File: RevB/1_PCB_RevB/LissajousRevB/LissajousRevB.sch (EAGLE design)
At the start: 77 parts, among them U101 LM348D, U201 LM348D, U401 LM348D

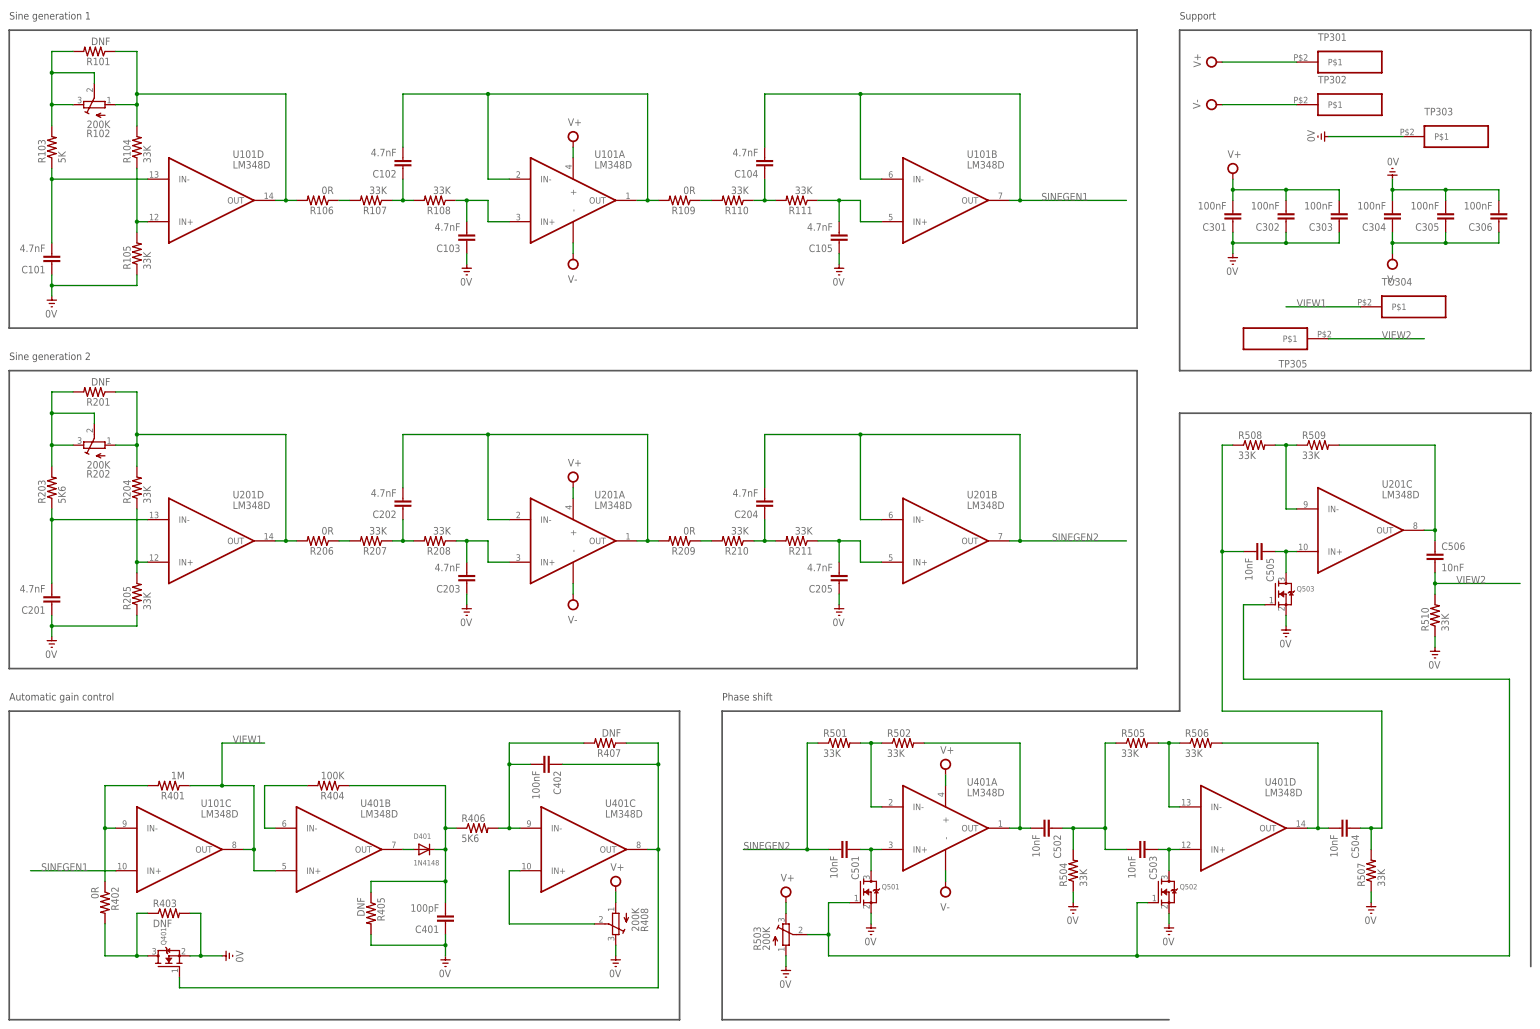
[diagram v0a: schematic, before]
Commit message: down to one quad op-amp package
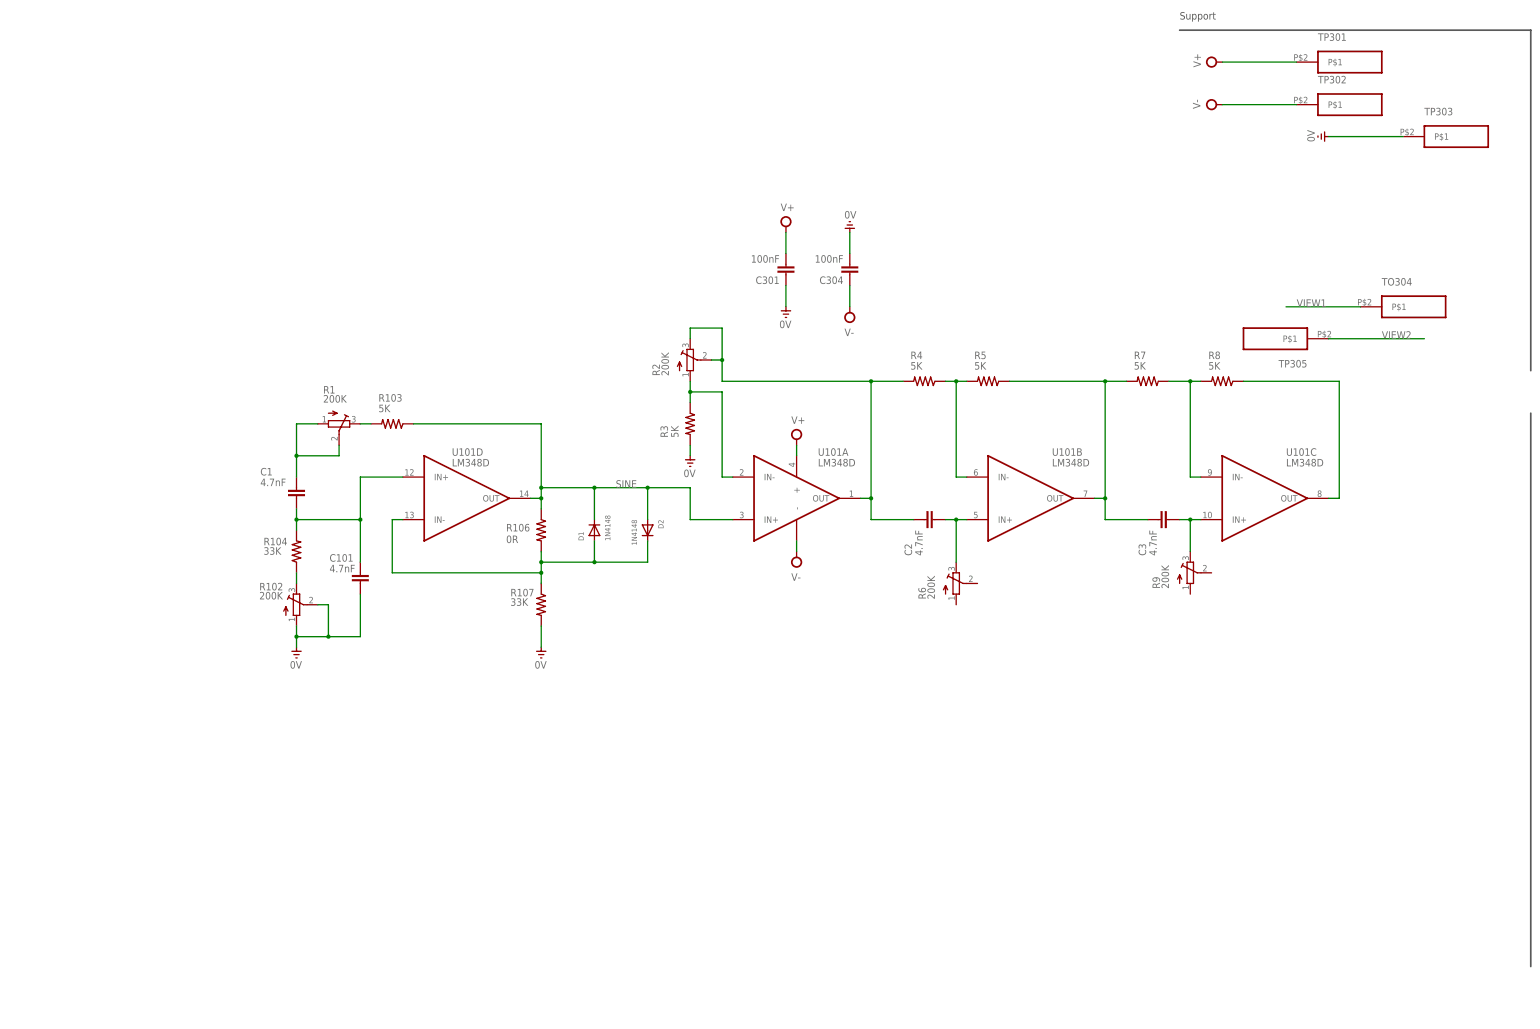
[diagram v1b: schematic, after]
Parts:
- removed C102, C103, C104, C105, C201, C202, C203, C204, C205: 4.7nF, passives:CAP0603-CAP
- removed C302, C303, C305, C306, C402: 100nF, passives:CAP0603-CAP
- removed C401: 100pF, passives:CAP0603-CAP
- removed C501, C502, C503, C504, C505, C506: 10nF, passives:CAP0603-CAP
- removed D401: 1N4148, adafruit:DIODESMA
- removed Q401, Q501, Q502, Q503: (no value), adafruit:MOSFET-NREFLOW
- removed R101, R201, R403, R405, R407: DNF, passives:RESISTOR0603-RES
- removed R105, R108, R110, R111, R204, R205, R207, R208, R210, R211, R501, R502, R504, R505, R506, R507, R508, R509, R510: 33K, passives:RESISTOR0603-RES
- removed R109, R206, R209, R402: 0R, passives:RESISTOR0603-RES
- removed R202, R408, R503: 200K, adafruit:TRIMPOTTC33X
- removed R203, R406: 5K6, passives:RESISTOR0603-RES
- removed R401: 1M, passives:RESISTOR0603-RES
- removed R404: 100K, passives:RESISTOR0603-RES
- removed U201, U401: LM348D, LM348D:LM348D
- added C1, C2, C3: 4.7nF, passives:CAP0603-CAP
- added D1, D2: 1N4148, adafruit:DIODESMA
- added R1, R2, R6, R9: 200K, adafruit:TRIMPOTTC33X
- added R3, R4, R5, R7, R8: 5K, passives:RESISTOR0603-RES
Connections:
- removed net N$11: C105.2, R111.1, U101B.IN+
- removed net N$13: R401.2, R402.1, U101C.IN-
- removed net N$14: R109.1, R110.2
- removed net N$16: C203.2, R208.1, U201A.IN+
- removed net N$20: C501.1, Q501.D, U401A.IN+
- removed net N$21: C202.2, R209.2, U201A.IN-, U201A.OUT
- removed net N$22: R206.1, R207.2
- removed net N$23: R209.1, R210.2
- removed net N$24: R201.2, R202.E, R202.S, R203.2
- removed net N$25: C402.2, R406.2, R407.2, U401C.IN-
- removed net N$26: R501.2, R502.1, U401A.IN-
- removed net N$27: R404.2, U401B.IN-
- removed net N$28: D401.A, U401B.OUT
- removed net N$29: C502.1, C503.2, R504.2, R505.1
- removed net N$30: C401.2, D401.C, R404.1, R405.1, R406.1
- removed net N$31: Q401.D, R402.2, R403.1
- removed net N$32: C402.1, Q401.G, R407.1, U401C.OUT
- removed net N$33: C502.2, R502.2, U401A.OUT
- removed net N$34: R408.S, U401C.IN+
- removed net N$36: C503.1, Q502.D, U401D.IN+
- removed net N$37: R505.2, R506.1, U401D.IN-
- removed net N$38: Q501.G, Q502.G, Q503.G, R503.S
- removed net N$39: C504.2, R506.2, U401D.OUT
- removed net N$40: R508.2, R509.1, U201C.IN-
- removed net N$42: C504.1, C505.2, R507.2, R508.1
- removed net N$45: C505.1, Q503.D, U201C.IN+
- removed net N$46: C506.1, R509.2, U201C.OUT
- removed net N$6: C102.1, R107.1, R108.2
- removed net N$8: C102.2, R109.2, U101A.IN-, U101A.OUT
- removed net SINEGEN1: C104.2, U101B.IN-, U101B.OUT, U101C.IN+
- removed net SINEGEN2: C204.2, C501.2, R501.1, U201B.IN-, U201B.OUT
- new net SINE: D1.C, D2.A, R103.1, R106.1, U101A.IN+, U101D.OUT
- net 0V: now also R102.A, R102.S, R107.2, R3.2; no longer C103.1, C105.1, C201.1, C203.1, C205.1, C302.1, C303.1, C305.2, C306.2, C401.1, Q401.S, Q501.S, Q502.S, Q503.S, R105.1, R205.1, R403.2, R405.2, R408.E, R503.A, R504.1, R507.1, R510.1
- net N$1: now also R1.E, R103.2; no longer C101.2, R103.1, U101D.IN-
- net N$10: now also C2.1, R6.E, U101B.IN+; no longer C201.2, R203.1, U201D.IN-
- net N$12: now also C2.2, R2.E, R2.S, R4.2, U101A.OUT; no longer C104.1, R110.1, R111.2
- net N$15: now also R7.1, R8.2, U101C.IN-; no longer R201.1, R202.A, R204.2, R206.2, U201D.OUT
- net N$17: now also C3.1, R9.E, U101C.IN+; no longer C202.1, R207.1, R208.2
- net N$18: now also R8.1, U101C.OUT; no longer C205.2, R211.1, U201B.IN+
- net N$19: now also C3.2, R5.1, R7.2, U101B.OUT; no longer C204.1, R210.1, R211.2
- net N$2: now also R102.E; no longer R105.2, U101D.IN+
- net N$3: now also D1.A, D2.C, R106.2, R107.1, U101D.IN-; no longer R106.1, R107.2
- net N$4: now also C1.2, R1.A, R1.S; no longer R101.2, R102.E, R102.S, R103.2
- net N$5: now also R2.A, R3.1, U101A.IN-; no longer C103.2, R108.1, U101A.IN+
- net N$7: now also C1.1, C101.2, U101D.IN+; no longer R101.1, R102.A, R106.2, U101D.OUT
- net N$9: now also R4.1, R5.2, U101B.IN-; no longer R204.1, R205.2, U201D.IN+
- net V+: no longer C302.2, C303.2, R408.A, R503.E, U201A.+, U401A.+
- net V-: no longer C305.1, C306.1, U201A.-, U401A.-
- net VIEW1: no longer R401.1, U101C.OUT, U401B.IN+
- net VIEW2: no longer C506.2, R510.2
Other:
- note removed: "Automatic gain control"
- note removed: "Phase shift"
- note removed: "Sine generation 1"
- note removed: "Sine generation 2"
- moved on the sheet: C101, C301, C304, R102, R103, R104, R106, R107, U101A, U101B, U101C, U101D

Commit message: core schematics done
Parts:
- removed C1, C2, C3: 4.7nF, passives:CAP0603-CAP
- removed D1, D2: 1N4148, adafruit:DIODESMA
- removed R1, R2, R9: 200K, adafruit:TRIMPOTTC33X
- removed R103, R3, R4, R5, R8: 5K, passives:RESISTOR0603-RES
- removed R107: 33K, passives:RESISTOR0603-RES
- removed TO304, TP301, TP302, TP303, TP305: PAD, pad:PAD
- added C11: 820pF, passives:CAP0603-CAP
- added C31, C41: 1.5nF, passives:CAP0603-CAP
- added D11, D12: 1N4148, adafruit:DIODESMA
- added R11, R23, R43: 200K, adafruit:TRIMPOTTC33X
- added R12: 15K, passives:RESISTOR0603-RES
- added R16: 47K, passives:RESISTOR0603-RES
- added R21, R22, R31, R32, R42: 10K, passives:RESISTOR0603-RES
- C12: value 4.7nF -> 820pF
- R13: value 33K -> 15K
- R15: value 0R -> 100K
- R41: value 5K -> 10K
- renumbered C101 to C12, R102 to R14, R104 to R13, R106 to R15, R6 to R33, R7 to R41, U101 to U1
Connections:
- removed net N$5: R2.A, R3.1, U1A.IN-
- removed net VIEW1: TO304.P$1
- removed net VIEW2: TP305.P$1
- new net N$6: R22.1, R23.A
- new net N$8: R21.1, R22.2, U1A.IN-
- net 0V: now also R16.2, R21.2, R33.A, R33.S, R43.A, R43.S; no longer R107.2, R3.2, TP303.P$1
- net N$1: now also R11.E, R12.2; no longer R1.E, R103.2
- net N$10: now also C31.1; no longer C2.1
- net N$12: now also C31.2, R23.E, R23.S, R31.2; no longer C2.2, R2.E, R2.S, R4.2
- net N$15: now also R42.2; no longer R8.2
- net N$17: now also C41.1, R43.E; no longer C3.1, R9.E
- net N$18: now also R42.1; no longer R8.1
- net N$19: now also C41.2, R32.1; no longer C3.2, R5.1
- net N$3: now also D11.A, D12.C, R16.1; no longer D1.A, D2.C, R107.1
- net N$4: now also C11.2, R11.A, R11.S; no longer C1.2, R1.A, R1.S
- net N$7: now also C11.1; no longer C1.1
- net N$9: now also R31.1, R32.2; no longer R4.1, R5.2
- net SINE: now also D11.C, D12.A, R12.1; no longer D1.C, D2.A, R103.1
- net V+: no longer TP301.P$1
- net V-: no longer TP302.P$1
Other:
- note added: "Amp (-1 to -21)"
- note added: "Phase shift (0 to 180)"
- note added: "Sine gen (1KHz to 12KHz)"
- note removed: "Support"
- moved on the sheet: C301, C304

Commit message: ready to route
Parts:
- added AMP, GND1, GND2, OUT, SINE, V1+, V1-, V2+, V2-: TESTPADS, TestPads:TESTPADS
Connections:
- net 0V: now also GND1.TP, GND2.TP
- net N$12: now also AMP.TP
- net N$18: now also OUT.TP
- net SINE: now also SINE.TP
- net V+: now also V1+.TP, V2+.TP
- net V-: now also V1-.TP, V2-.TP
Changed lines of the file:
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@@
 <part name="V2" library="supply" deviceset="0V" device=""/>
 <part name="R22" library="passives" deviceset="RESISTOR" device="0603-RES" value="10K"/>
+<part name="V7" library="supply" deviceset="0V" device=""/>
+<part name="V8" library="supply" deviceset="V-" device=""/>
+<part name="V9" library="supply" deviceset="V+" device=""/>
+<part name="V1+" library="TestPads" deviceset="TESTPADS" device=""/>
+<part name="GND1" library="TestPads" deviceset="TESTPADS" device=""/>
+<part name="V1-" library="TestPads" deviceset="TESTPADS" device=""/>
+<part name="V2+" library="TestPads" deviceset="TESTPADS" device=""/>
+<part name="GND2" library="TestPads" deviceset="TESTPADS" device=""/>
+<part name="V2-" library="TestPads" deviceset="TESTPADS" device=""/>
+<part name="SINE" library="TestPads" deviceset="TESTPADS" device=""/>
+<part name="AMP" library="TestPads" deviceset="TESTPADS" device=""/>
+<part name="OUT" library="TestPads" deviceset="TESTPADS" device=""/>
 </parts>
 <sheets>
@@
 <attribute name="VALUE" x="185.42" y="167.64" size="1.778" layer="96"/>
 </instance>
+<instance part="V7" gate="1" x="165.1" y="45.72"/>
+<instance part="V8" gate="1" x="180.34" y="55.88" rot="R180"/>
+<instance part="V9" gate="1" x="149.86" y="55.88"/>
+<instance part="V1+" gate="G$1" x="157.48" y="55.88" smashed="yes" rot="R270">
+<attribute name="NAME" x="154.94" y="71.12" size="1.27" layer="95"/>
+</instance>
+<instance part="GND1" gate="G$1" x="172.72" y="55.88" smashed="yes" rot="R270">
+<attribute name="NAME" x="170.18" y="71.12" size="1.27" layer="95"/>
+</instance>
+<instance part="V1-" gate="G$1" x="187.96" y="55.88" smashed="yes" rot="R270">
+<attribute name="NAME" x="185.42" y="71.12" size="1.27" layer="95"/>
+</instance>
+<instance part="V2+" gate="G$1" x="157.48" y="45.72" smashed="yes" rot="R90">
+<attribute name="NAME" x="154.94" y="30.48" size="1.27" layer="95"/>
+</instance>
+<instance part="GND2" gate="G$1" x="172.72" y="45.72" smashed="yes" rot="R90">
+<attribute name="NAME" x="170.18" y="30.48" size="1.27" layer="95"/>
+</instance>
+<instance part="V2-" gate="G$1" x="187.96" y="45.72" smashed="yes" rot="R90">
+<attribute name="NAME" x="185.42" y="30.48" size="1.27" layer="95"/>
+</instance>
+<instance part="SINE" gate="G$1" x="175.26" y="127" smashed="yes" rot="R90">
+<attribute name="NAME" x="172.72" y="111.76" size="1.27" layer="95"/>
+</instance>
+<instance part="AMP" gate="G$1" x="208.28" y="127" smashed="yes" rot="R90">
+<attribute name="NAME" x="205.74" y="111.76" size="1.27" layer="95"/>
+</instance>
+<instance part="OUT" gate="G$1" x="332.74" y="137.16" smashed="yes" rot="R180">
+<attribute name="NAME" x="347.98" y="137.16" size="1.27" layer="95"/>
+</instance>
 </instances>
 <busses>
@@
 <wire x1="213.36" y1="238.76" x2="213.36" y2="236.22" width="0.1524" layer="91"/>
 </segment>
+<segment>
+<pinref part="V8" gate="1" pin="V-"/>
+<wire x1="180.34" y1="53.34" x2="180.34" y2="50.8" width="0.1524" layer="91"/>
+<wire x1="187.96" y1="45.72" x2="187.96" y2="50.8" width="0.1524" layer="91"/>
+<wire x1="187.96" y1="50.8" x2="187.96" y2="55.88" width="0.1524" layer="91"/>
+<wire x1="180.34" y1="50.8" x2="187.96" y2="50.8" width="0.1524" layer="91"/>
+<junction x="187.96" y="50.8"/>
+<pinref part="V1-" gate="G$1" pin="TP"/>
+<pinref part="V2-" gate="G$1" pin="TP"/>
+</segment>
 </net>
 <net name="V+" class="0">
@@
 <pinref part="C301" gate="G$1" pin="2"/>
 <wire x1="190.5" y1="236.22" x2="190.5" y2="238.76" width="0.1524" layer="91"/>
+</segment>
+<segment>
+<pinref part="V9" gate="1" pin="V+"/>
+<wire x1="149.86" y1="53.34" x2="149.86" y2="50.8" width="0.1524" layer="91"/>
+<wire x1="157.48" y1="45.72" x2="157.48" y2="50.8" width="0.1524" layer="91"/>
+<wire x1="157.48" y1="50.8" x2="157.48" y2="55.88" width="0.1524" layer="91"/>
+<wire x1="149.86" y1="50.8" x2="157.48" y2="50.8" width="0.1524" layer="91"/>
+<junction x="157.48" y="50.8"/>
+<pinref part="V1+" gate="G$1" pin="TP"/>
+<pinref part="V2+" gate="G$1" pin="TP"/>
 </segment>
 </net>
@@
 <pinref part="V6" gate="1" pin="0V"/>
 <wire x1="165.1" y1="165.1" x2="165.1" y2="162.56" width="0.1524" layer="91"/>
+</segment>
+<segment>
+<pinref part="V7" gate="1" pin="0V"/>
+<wire x1="165.1" y1="48.26" x2="165.1" y2="50.8" width="0.1524" layer="91"/>
+<wire x1="172.72" y1="45.72" x2="172.72" y2="50.8" width="0.1524" layer="91"/>
+<wire x1="172.72" y1="50.8" x2="172.72" y2="55.88" width="0.1524" layer="91"/>
+<wire x1="165.1" y1="50.8" x2="172.72" y2="50.8" width="0.1524" layer="91"/>
+<junction x="172.72" y="50.8"/>
+<pinref part="GND1" gate="G$1" pin="TP"/>
+<pinref part="GND2" gate="G$1" pin="TP"/>
 </segment>
 </net>
@@
 <pinref part="U1" gate="A" pin="IN+"/>
 <wire x1="175.26" y1="132.08" x2="182.88" y2="132.08" width="0.1524" layer="91"/>
+<wire x1="175.26" y1="127" x2="175.26" y2="132.08" width="0.1524" layer="91"/>
+<junction x="175.26" y="132.08"/>
+<pinref part="SINE" gate="G$1" pin="TP"/>
 </segment>
 </net>
@@
 <pinref part="R42" gate="G$1" pin="1"/>
 <wire x1="327.66" y1="165.1" x2="314.96" y2="165.1" width="0.1524" layer="91"/>
+<wire x1="332.74" y1="137.16" x2="327.66" y2="137.16" width="0.1524" layer="91"/>
+<junction x="327.66" y="137.16"/>
+<pinref part="OUT" gate="G$1" pin="TP"/>
 </segment>
 </net>
@@
 <wire x1="208.28" y1="157.48" x2="215.9" y2="157.48" width="0.1524" layer="91"/>
 <junction x="215.9" y="157.48"/>
-</segment>
-</net>
+<wire x1="215.9" y1="132.08" x2="208.28" y2="132.08" width="0.1524" layer="91"/>
+<junction x="215.9" y="132.08"/>
+<wire x1="208.28" y1="132.08" x2="208.28" y2="127" width="0.1524" layer="91"/>
+<pinref part="AMP" gate="G$1" pin="TP"/>
+</segment>
+</net>
